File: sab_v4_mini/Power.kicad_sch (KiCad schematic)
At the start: 126 parts, among them J3 Barrel_Jack_Switch, U1 IS42S16100H-7TL, U2 OP275, U20 AP1117-33, U3 7909, U4 OP275, U5 AP1117-33, U6 7809, U9 AP1117-33

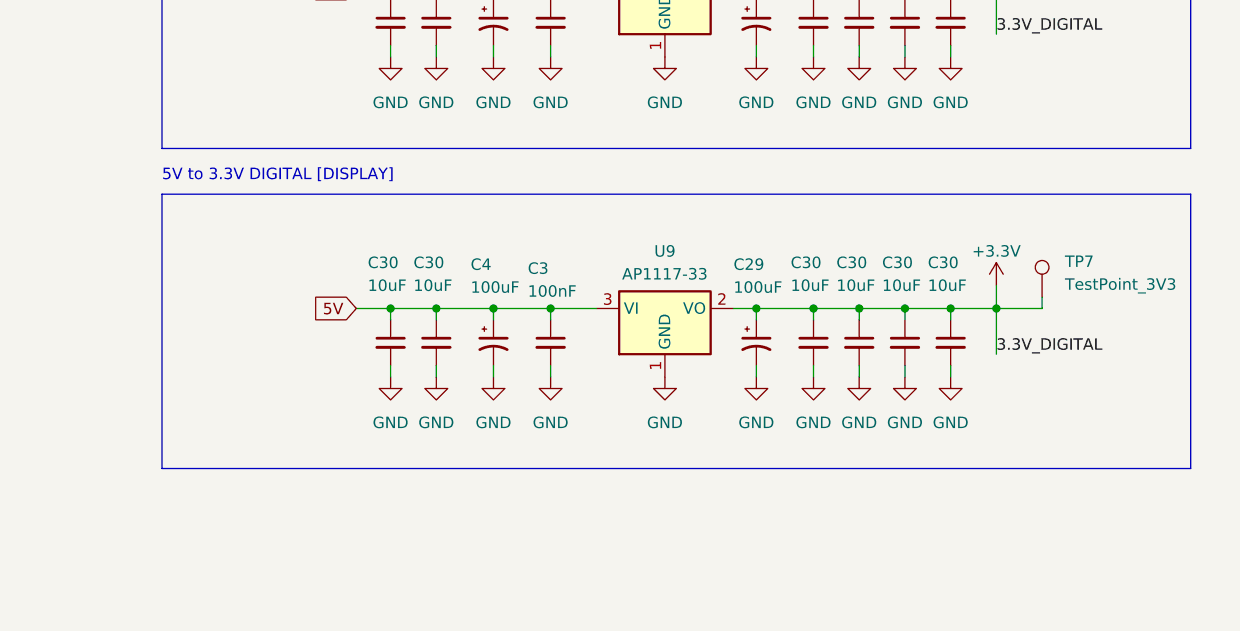
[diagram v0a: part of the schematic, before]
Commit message: Delete unused pages
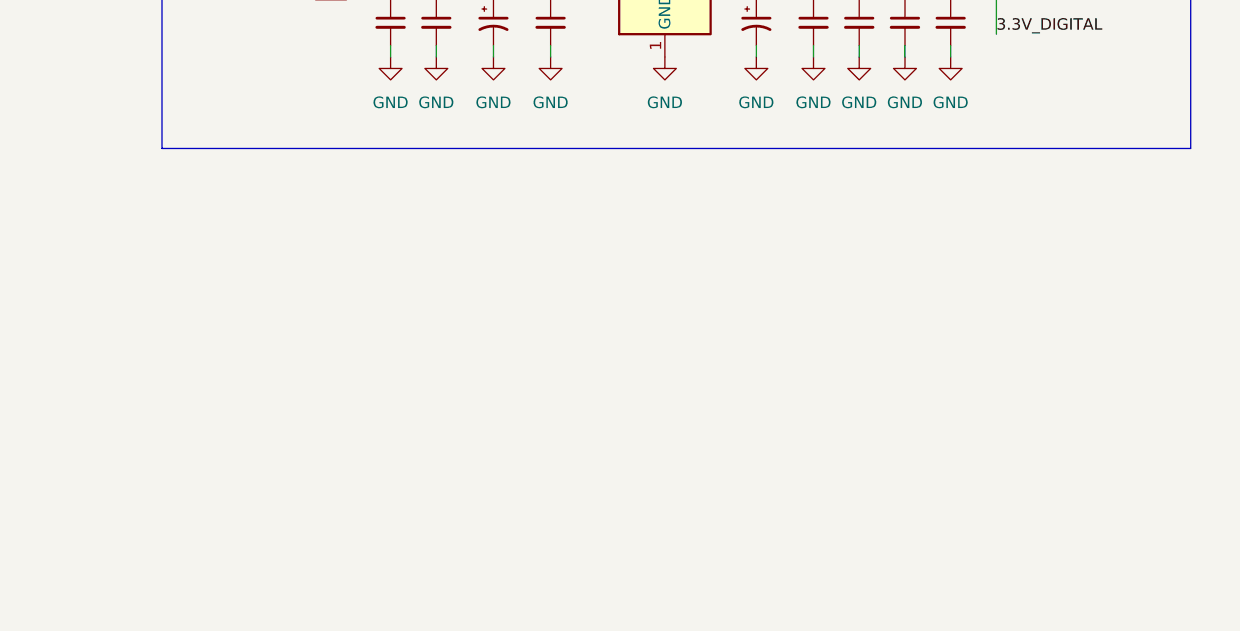
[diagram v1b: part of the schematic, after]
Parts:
- removed C29, C4: 100uF, stm_audio_board_footprints:CP_Radial_D6.3mm_P2.50mm_reference_fix, symbol Device:C_Polarized_Small_US
- removed C3: 100nF, Capacitor_SMD:C_0603_1608Metric, symbol Device:C_Small
- removed C30 (x6): 10uF, Capacitor_SMD:C_1206_3216Metric, symbol Device:C_Small
- removed TP7: TestPoint_3V3, TestPoint:TestPoint_Pad_D1.5mm, symbol Connector:TestPoint
- removed U9: AP1117-33, Package_TO_SOT_SMD:SOT-223, symbol Regulator_Linear:AP1117-33
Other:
- note removed: "5V to 3.3V DIGITAL [DISPLAY]"

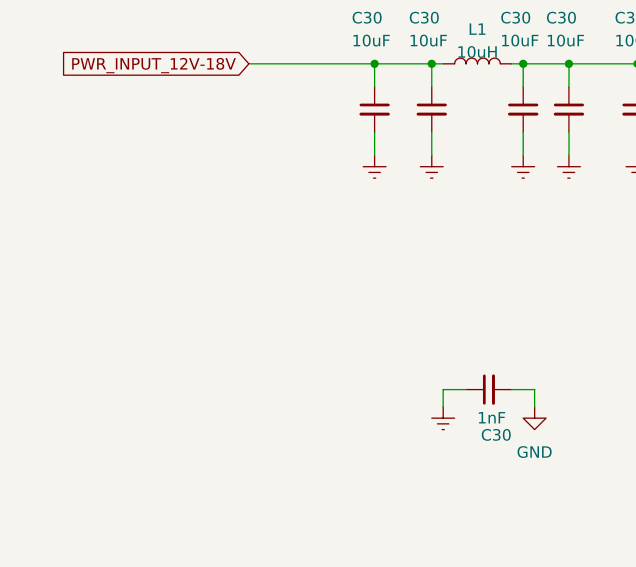
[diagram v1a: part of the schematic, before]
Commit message: deleted unused pin added mcu
stm32h750vbt6
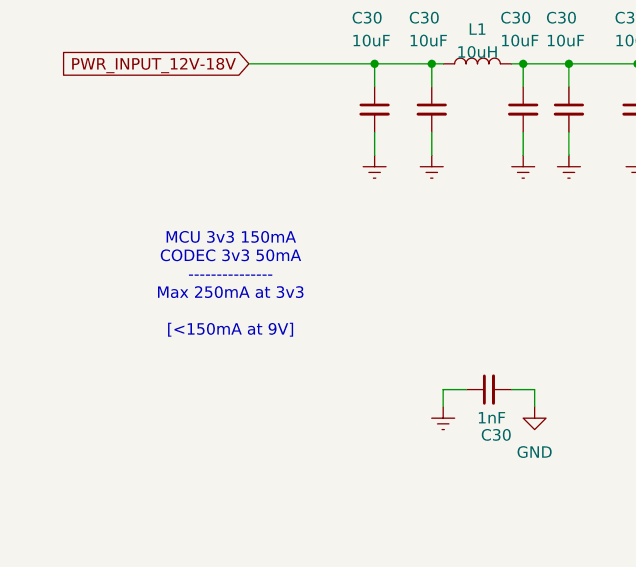
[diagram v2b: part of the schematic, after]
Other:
- note added: "MCU 3v3 150mA CODEC 3v3 50mA --------------- Max 250mA at 3v3 [<150mA at 9V]"
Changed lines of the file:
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@@
+		)
+	)
+	(text "MCU 3v3 150mA\nCODEC 3v3 50mA\n---------------\nMax 250mA at 3v3\n\n[<150mA at 9V]"
+		(exclude_from_sim no)
+		(at 39.878 109.728 0)
+		(effects
+			(font
+				(size 1.27 1.27)
+			)
 		)
 	)
